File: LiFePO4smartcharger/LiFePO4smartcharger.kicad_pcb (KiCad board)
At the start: 2 copper layers, 99.3 x 98.6 mm, 95 parts, among them J1 Conn_01x02, J10 Conn_01x01, J11 Conn_01x01, J12 Conn_01x04, J2 Conn_02x03_Odd_Even, J3 Conn_01x02, J4 Conn_01x02, J5 Barrel_Jack, J6 Conn_01x01, J7 Conn_01x01, J8 Conn_01x02, J9 Conn_01x02, Q1 TIP42, Q2 TIP41, Q4 TIP41C, T1 Transformer_1P1Sdotted, U1 ATMEGA328P-PU, U2 LM358, U3 LCD-016N002L, U4 TL494, U9 LM7805_TO220, X3 16MHz

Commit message: Added important shutdown feature
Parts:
- added D4: 1N4744A, Diodes_THT:D_DO-41_SOD81_P7.62mm_Horizontal, F.Cu at (59.7, 33.1)
- added D8: 1N4148, Diodes_THT:D_DO-35_SOD27_P7.62mm_Horizontal, F.Cu at (90.3, 102.0)
- moved C2 15.1 mm to (80.7, 111.3), turned to 270 degrees
- moved J1 5.40 mm to (91.7, 35.7), turned to 0 degrees
- moved J3 5.20 mm to (81.2, 35.7), turned to 0 degrees
- moved C9 5.00 mm to (76.7, 40.1), turned to 90 degrees
- moved R3 1.33 mm to (82.4, 108.2)
- moved R24 1.28 mm to (102.9, 76.0)
- moved T1 1.28 mm to (94.4, 63.0), turned to 270 degrees
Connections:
- T1 pad 1: Net-(C13-Pad1) -> GND
- T1 pad 2: GND -> CURRENTSHUNT
- T1 pad 3: Net-(C9-Pad1) -> Net-(C13-Pad1)
- T1 pad 4: CURRENTSHUNT -> Net-(C9-Pad1)
- U1 pad 6: (no net) -> SHUTDOWN
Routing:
- net SHUTDOWN: track 0.00 -> 73.5 mm
- net Net-(C2-Pad1): track 36.5 -> 49.8 mm
- net CURRENTSHUNT: track 140.8 -> 128.0 mm
- net Net-(C13-Pad1): track 72.6 -> 84.4 mm
- net Net-(C10-Pad2): track 46.0 -> 57.7 mm
- net Net-(C9-Pad1): track 48.9 -> 41.0 mm
- net +24V: track 212.7 -> 209.8 mm
- net Net-(C12-Pad1): track 71.5 -> 72.3 mm
- net A0: track 78.7 -> 78.0 mm
- removed copper zone on B.Cu, net CURRENTSHUNT
- removed copper zone on B.Cu, net Net-(C13-Pad1)

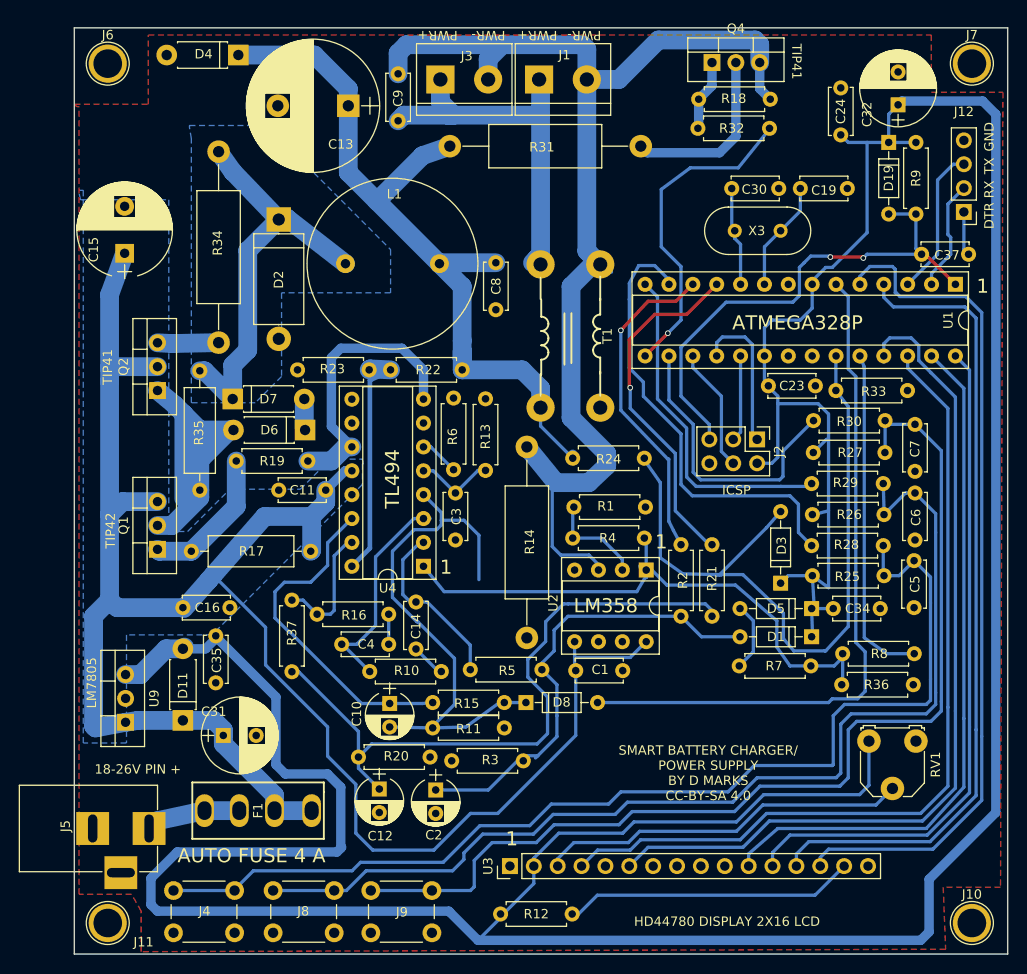
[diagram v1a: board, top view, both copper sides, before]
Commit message: Changed to pulse to pulse shut off
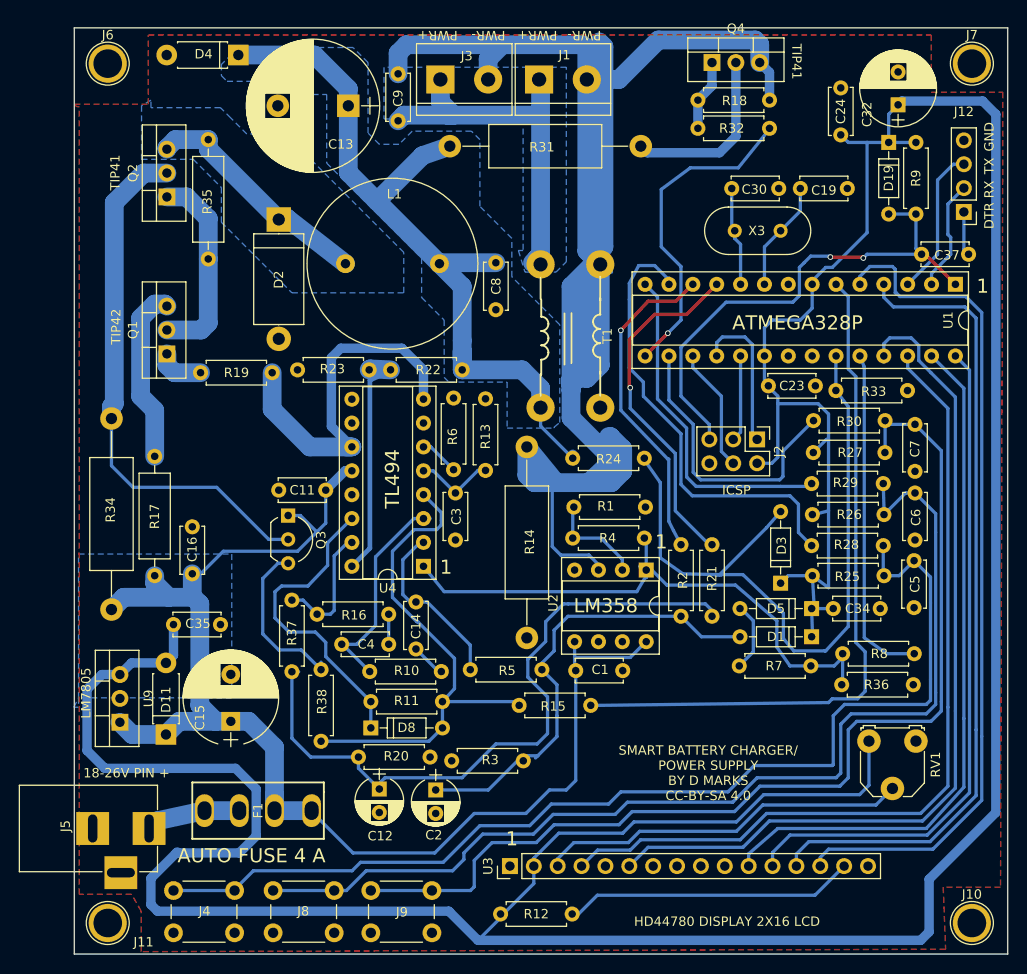
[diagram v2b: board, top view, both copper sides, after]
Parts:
- removed C10: 10 uF, Capacitors_THT:CP_Radial_D5.0mm_P2.50mm
- removed C31: 100uF, Capacitors_THT:CP_Radial_D8.0mm_P3.50mm
- removed D6, D7: 1N4007, Diodes_THT:D_DO-41_SOD81_P7.62mm_Horizontal
- added Q3: 2N3906, TO_SOT_Packages_THT:TO-92_Inline_Wide, F.Cu at (65.0, 82.1)
- added R38: 4k7, Resistors_THT:R_Axial_DIN0207_L6.3mm_D2.5mm_P7.62mm_Horizontal, F.Cu at (68.5, 98.5)
- R11: value 1k -> 100k
- moved C15 51.1 mm to (58.9, 104.0)
- moved R34 30.6 mm to (46.2, 92.1)
- moved R35 24.6 mm to (56.5, 54.8)
- moved Q1 20.8 mm to (52.1, 64.9)
- moved Q2 20.6 mm to (52.1, 48.2)
- moved D8 16.7 mm to (73.8, 104.7)
- moved R11 14.5 mm to (73.8, 101.9), turned to 0 degrees
- moved R17 10.8 mm to (50.8, 75.8), turned to 270 degrees
- moved R19 10.1 mm to (63.3, 66.9)
- moved R15 9.20 mm to (97.2, 102.3)
- moved R18 7.70 mm to (108.6, 37.9), turned to 0 degrees
- moved C35 4.66 mm to (52.8, 93.7), turned to 0 degrees
- moved C16 3.74 mm to (54.8, 88.3), turned to 90 degrees
- moved D11 2.34 mm to (52.0, 105.4)
- moved U9 0.60 mm to (47.1, 104.1)
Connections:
- D8 pad 1: Net-(C10-Pad2) -> Net-(D8-Pad1)
- D8 pad 2: SHUTDOWN -> Net-(D8-Pad2)
- Q1 pad 3: +24V -> Net-(Q1-Pad3)
- Q2 pad 2: +24V -> Net-(Q2-Pad2)
- Q2 pad 3: Net-(Q2-Pad3) -> Net-(D2-Pad1)
- R11 pad 1: GND -> Net-(D8-Pad1)
- R11 pad 2: Net-(C10-Pad2) -> Net-(D8-Pad2)
- R15 pad 1: Net-(C10-Pad2) -> SHUTDOWN
- R15 pad 2: Net-(C10-Pad1) -> Net-(D8-Pad2)
- R17 pad 1: Net-(Q1-Pad1) -> Net-(Q1-Pad3)
- R18 pad 1: CURRENTSHUNT -> Net-(Q4-Pad1)
- R18 pad 2: Net-(Q4-Pad1) -> CURRENTSHUNT
- R34 pad 1: Net-(Q2-Pad3) -> +24V
- R34 pad 2: Net-(D2-Pad1) -> Net-(Q2-Pad2)
- U4 pad 14: Net-(C10-Pad1) -> Net-(D8-Pad1)
- U4 pad 4: Net-(C10-Pad2) -> Net-(D8-Pad2)
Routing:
- net CURRENTSHUNT: track 128.0 -> 194.6 mm
- net +24V: track 209.8 -> 143.7 mm
- net Net-(Q2-Pad2): track 0.00 -> 57.8 mm
- net Net-(C10-Pad2): track 57.7 -> 0.00 mm
- net Net-(D8-Pad2): track 0.00 -> 54.6 mm
- net Net-(C10-Pad1): track 36.2 -> 0.00 mm
- net Net-(D8-Pad1): track 0.00 -> 33.2 mm
- net Net-(D2-Pad1): track 44.4 -> 25.3 mm
- net Net-(Q1-Pad3): track 0.00 -> 18.8 mm
- net Net-(Q3-Pad3): track 0.00 -> 17.8 mm
- net Net-(Q1-Pad2): track 36.6 -> 21.2 mm
- net Net-(Q1-Pad1): track 15.3 -> 5.11 mm
- net Net-(R19-Pad1): track 30.0 -> 39.4 mm
- net Net-(Q2-Pad3): track 6.50 -> 0.00 mm
- net +5V: track 409.2 -> 403.2 mm
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- added copper zone on B.Cu, net Net-(C13-Pad1)

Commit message: Oops moved resistor in TIP42
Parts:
- moved R17 8.13 mm to (56.5, 70.0)
- moved C16 4.19 mm to (51.3, 90.6)
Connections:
- Q2 pad 2: Net-(Q2-Pad2) -> Net-(Q1-Pad3)
- Q3 pad 2: Net-(Q2-Pad2) -> Net-(Q1-Pad3)
- R17 pad 1: Net-(Q1-Pad3) -> Net-(Q1-Pad1)
- R17 pad 2: +24V -> Net-(Q1-Pad3)
- R34 pad 2: Net-(Q2-Pad2) -> Net-(Q1-Pad3)
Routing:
- net Net-(Q1-Pad3): track 18.8 -> 83.5 mm
- net Net-(Q2-Pad2): track 57.8 -> 0.00 mm
- net +24V: track 143.7 -> 140.3 mm
- net Net-(Q1-Pad1): track 5.11 -> 8.55 mm
- net Net-(Q1-Pad2): track 21.2 -> 20.3 mm
- added copper zone on B.Cu, net Net-(Q1-Pad2)
- added copper zone on B.Cu, net Net-(Q1-Pad3)

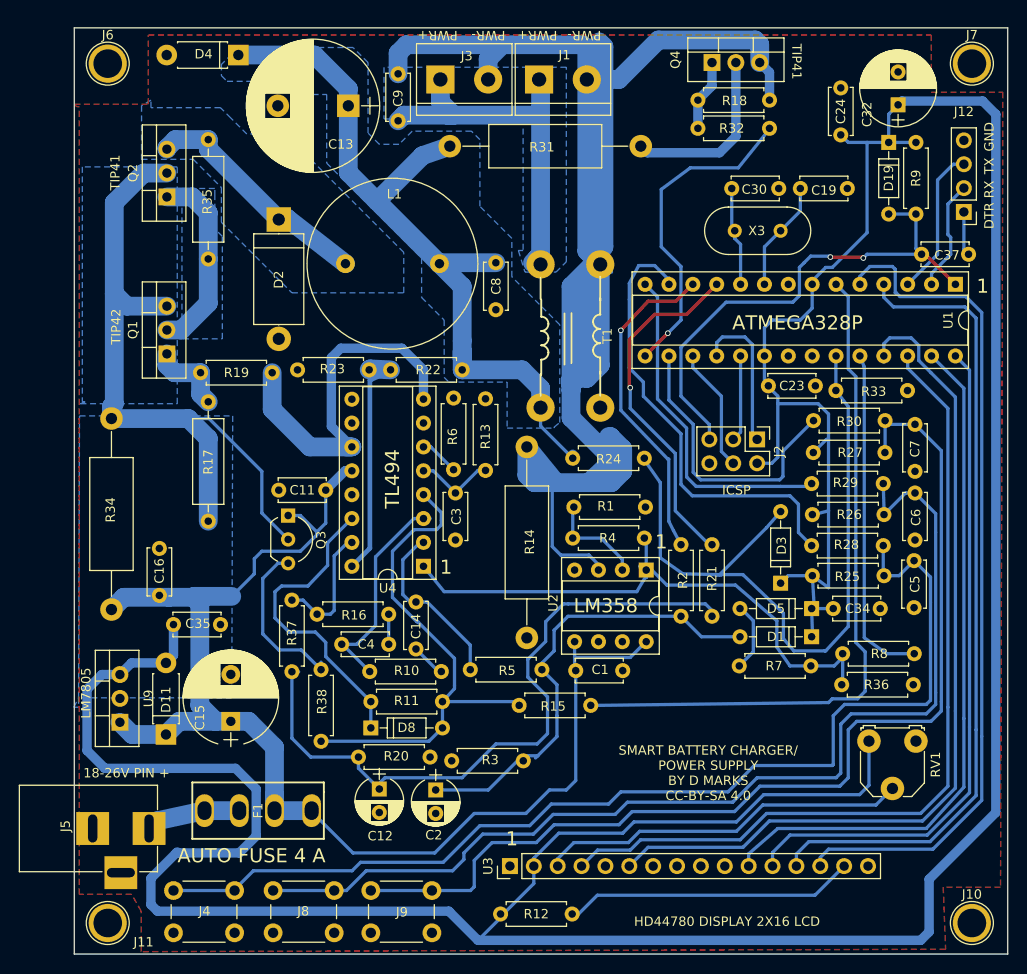
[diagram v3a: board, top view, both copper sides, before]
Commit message: Cleaned up layout
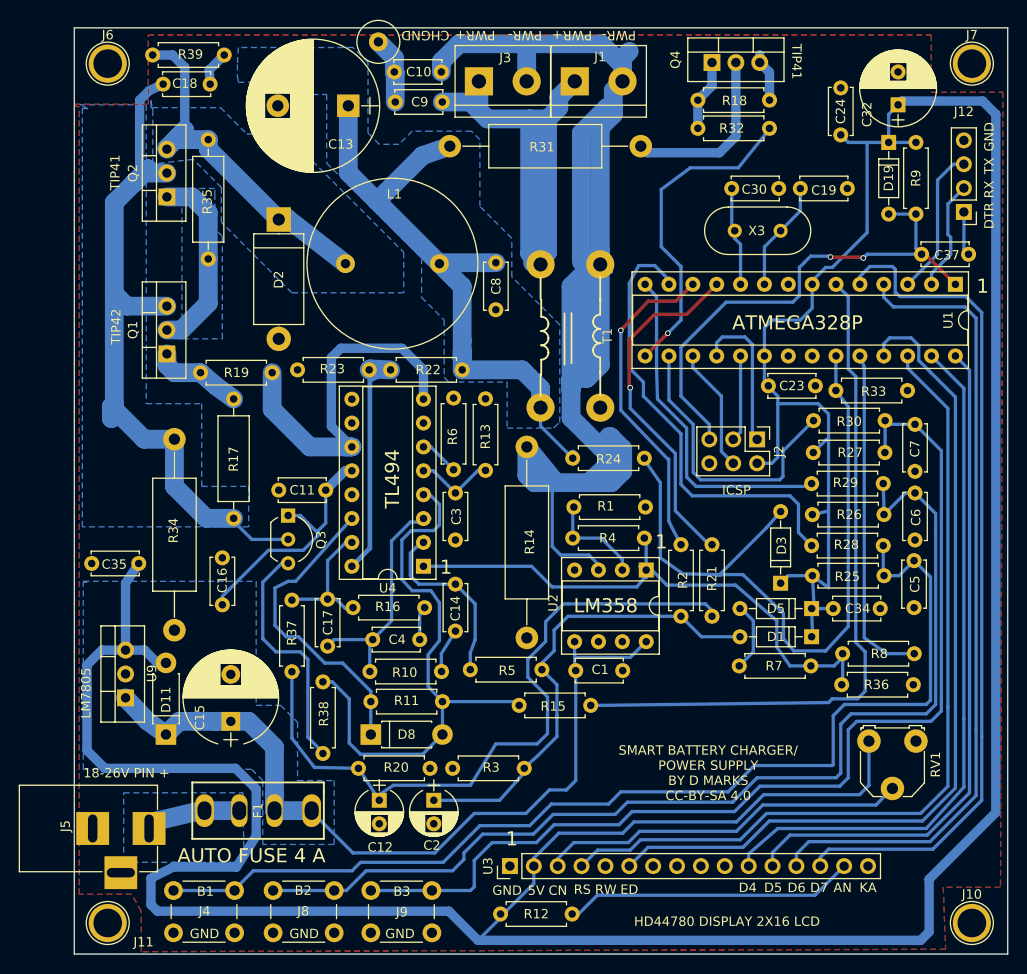
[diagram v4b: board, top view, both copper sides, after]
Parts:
- removed D4: 1N4744A, Diodes_THT:D_DO-41_SOD81_P7.62mm_Horizontal
- added C10: 100nF, Capacitors_THT:C_Disc_D5.0mm_W2.5mm_P5.00mm, F.Cu at (76.3, 34.9)
- added C17: 56 pF, Capacitors_THT:C_Disc_D5.0mm_W2.5mm_P5.00mm, F.Cu at (69.2, 91.0)
- added C18: NC, Capacitors_THT:C_Disc_D5.0mm_W2.5mm_P5.00mm, F.Cu at (56.7, 36.2)
- added J13: Conn_01x01, Connectors:1pin, F.Cu at (74.6, 31.7)
- added R39: NC, Resistors_THT:R_Axial_DIN0207_L6.3mm_D2.5mm_P7.62mm_Horizontal, F.Cu at (58.2, 33.1)
- D8: footprint Diodes_THT:D_DO-35_SOD27_P7.62mm_Horizontal -> Diodes_THT:D_DO-41_SOD81_P7.62mm_Horizontal
- F1: value Fuse -> SL-506P
- moved R10 7.60 mm to (73.7, 98.7), turned to 0 degrees
- moved C35 7.48 mm to (49.1, 87.2), turned to 180 degrees
- moved R34 7.05 mm to (52.9, 94.3)
- moved C16 6.77 mm to (58.0, 91.6)
- moved C9 5.11 mm to (81.4, 38.1), turned to 180 degrees
- moved C14 4.61 mm to (82.8, 94.4)
- moved J3 4.10 mm to (85.3, 35.9)
- moved R16 3.86 mm to (71.9, 91.9), turned to 0 degrees
- moved J1 3.81 mm to (95.5, 35.9)
- moved C4 3.34 mm to (79.0, 95.3)
- moved R17 2.72 mm to (59.2, 69.7)
- moved U9 2.67 mm to (47.7, 101.5)
- moved R38 1.32 mm to (68.7, 99.8)
- moved C12 1.20 mm to (74.7, 112.4)
- moved R20 1.20 mm to (80.1, 109.0)
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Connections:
- C4 pad 2: Net-(C4-Pad2) -> Net-(C17-Pad2)
- C9 pad 2: CURRENTSHUNT -> Net-(C10-Pad1)
- Q4 pad 3: CURRENTSHUNT -> Net-(Q4-Pad3)
- R10 pad 1: Net-(C14-Pad1) -> Net-(C17-Pad2)
- R10 pad 2: Net-(C4-Pad2) -> Net-(C14-Pad1)
- R16 pad 1: Net-(C4-Pad1) -> Net-(C17-Pad1)
- R16 pad 2: Net-(R16-Pad2) -> Net-(C4-Pad1)
- R18 pad 2: CURRENTSHUNT -> Net-(Q4-Pad3)
- R37 pad 1: Net-(R16-Pad2) -> Net-(C17-Pad1)
- R38 pad 1: Net-(Q3-Pad3) -> Net-(D8-Pad2)
- R38 pad 2: Net-(D8-Pad2) -> Net-(Q3-Pad3)
- U4 pad 15: Net-(R16-Pad2) -> Net-(C17-Pad1)
- U4 pad 3: Net-(C4-Pad2) -> Net-(C17-Pad2)
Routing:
- net CURRENTSHUNT: track 194.6 -> 164.8 mm
- net Net-(C17-Pad2): track 0.00 -> 26.2 mm
- net +24V: track 140.3 -> 114.4 mm
- net Net-(C4-Pad2): track 23.9 -> 0.00 mm
- net Net-(D2-Pad1): track 25.3 -> 40.8 mm
- net Net-(C17-Pad1): track 0.00 -> 15.1 mm
- net Net-(C13-Pad1): track 84.4 -> 69.5 mm
- net Net-(R16-Pad2): track 13.8 -> 0.00 mm
- net Net-(C9-Pad1): track 41.0 -> 52.9 mm
- net +5V: track 403.2 -> 411.3 mm
- net Net-(Q3-Pad3): track 17.8 -> 25.9 mm
- net Net-(D8-Pad2): track 54.6 -> 62.3 mm
- net Net-(C10-Pad1): track 0.00 -> 7.15 mm
- net Net-(Q4-Pad3): track 0.00 -> 5.25 mm
- net Net-(C18-Pad2): track 83.5 -> 78.8 mm
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- added copper zone on B.Cu, net Net-(F1-Pad2)
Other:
- board text added: "5V"
- board text added: "AN"
- board text added: "B1"
- board text added: "B2"
- board text added: "B3"
- board text added: "CHGND"
- board text added: "CN"
- board text added: "D4"
- board text added: "D5"
- board text added: "D6"
- board text added: "D7"
- board text added: "ED"
- board text added: "KA"
- board text added: "RS"
- board text added: "RW"

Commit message: Cleaned up the layout more
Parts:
- D1, D3, D5: footprint Diodes_THT:D_DO-35_SOD27_P7.62mm_Horizontal -> Diodes_THT:D_DO-41_SOD81_P7.62mm_Horizontal
- R35: value 100R -> 33R
- R6: value 47k -> 10k
- moved R38 7.60 mm to (68.7, 107.4), turned to 90 degrees
- moved C11 2.10 mm to (69.0, 77.3)
- moved R7 1.60 mm to (113.1, 99.7)
- moved D1 1.40 mm to (120.7, 96.4)
- moved D5 0.71 mm to (120.8, 92.7)
- moved C34 0.60 mm to (123.6, 92.0)
- moved D3 0.41 mm to (117.3, 88.9)
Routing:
- net Net-(Q3-Pad3): track 25.9 -> 18.5 mm
- net Net-(R19-Pad1): track 39.4 -> 32.3 mm
- net Net-(D8-Pad2): track 62.3 -> 57.3 mm
- net A0: track 78.0 -> 80.5 mm
- net Net-(D5-Pad2): track 7.38 -> 9.59 mm
- net Net-(C2-Pad1): track 51.1 -> 53.0 mm
- net Net-(R36-Pad1): track 63.6 -> 65.5 mm
- net +24V: track 114.4 -> 115.6 mm
- net +5V: track 411.3 -> 412.1 mm

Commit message: A few tweaks
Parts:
- added R40: 10k, Resistors_THT:R_Axial_DIN0207_L6.3mm_D2.5mm_P7.62mm_Horizontal, F.Cu at (61.3, 77.1)
- D1, D3, D5, D8: value 1N4148 -> 1N5819
- D2: value 1N5404 -> SB580
- R19: footprint Resistors_THT:R_Axial_DIN0207_L6.3mm_D2.5mm_P7.62mm_Horizontal -> Resistors_THT:R_Axial_DIN0309_L9.0mm_D3.2mm_P12.70mm_Horizontal
- moved R19 6.56 mm to (69.0, 70.2)
- moved R17 3.79 mm to (57.8, 73.2)
- moved D2 3.22 mm to (63.6, 47.4)
- moved C16 3.02 mm to (60.6, 90.2), turned to 270 degrees
- moved R36 0.14 mm to (124.0, 100.0)
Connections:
- Q3 pad 2: Net-(C18-Pad2) -> Net-(Q3-Pad2)
- Q4 pad 1: Net-(Q4-Pad1) -> CURRENTSHUNT
- R18 pad 1: Net-(Q4-Pad1) -> CURRENTSHUNT
- R32 pad 1: Net-(Q4-Pad1) -> CURRENTSHUNT
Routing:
- net CURRENTSHUNT: track 164.8 -> 181.2 mm
- net SHUTDOWN: track 73.6 -> 81.7 mm
- net Net-(Q4-Pad1): track 7.60 -> 0.00 mm
- net Net-(R19-Pad1): track 32.3 -> 26.1 mm
- net Net-(Q3-Pad2): track 0.00 -> 3.73 mm
- net +24V: track 115.6 -> 112.7 mm
- net Net-(C18-Pad2): track 78.8 -> 77.2 mm
- net Net-(Q1-Pad1): track 9.61 -> 10.6 mm
